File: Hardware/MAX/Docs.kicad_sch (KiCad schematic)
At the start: 0 parts

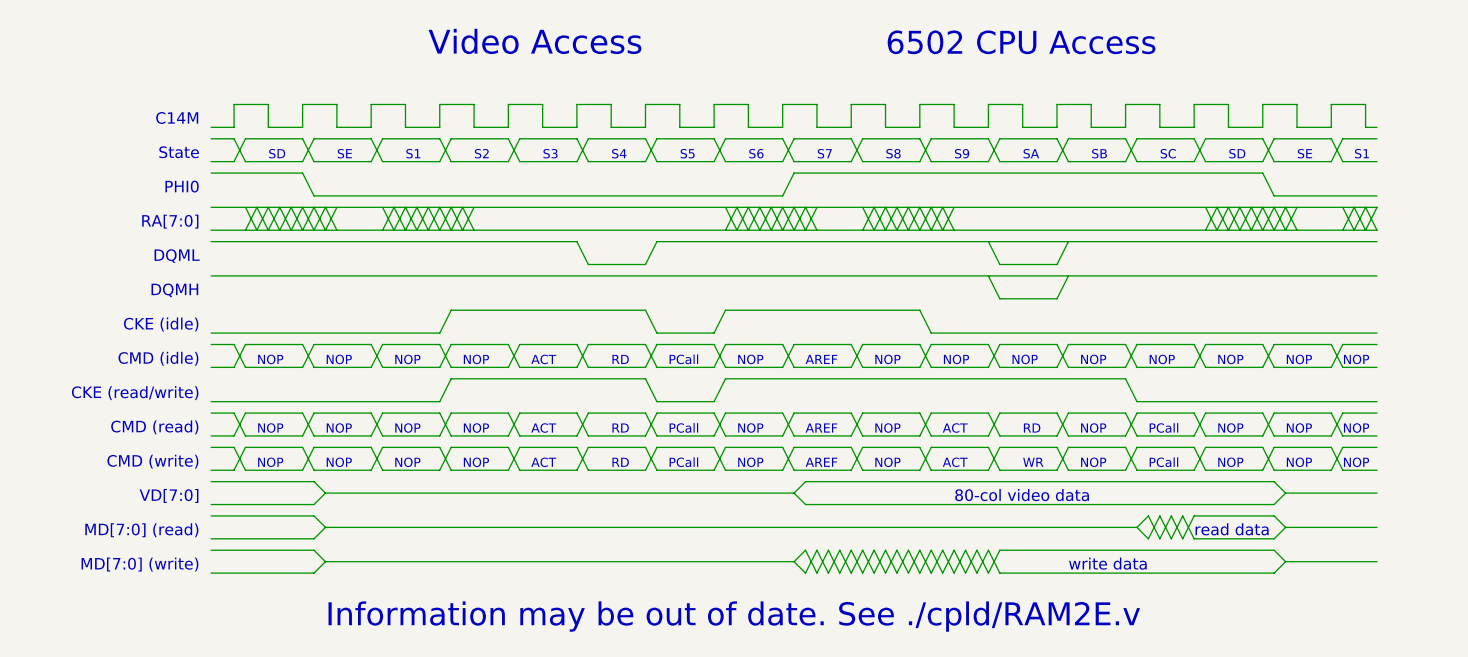
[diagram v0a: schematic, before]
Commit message: Revert "As sent to testers"
This reverts commit 4249ebe98332ad6fb679362fa153720a3e50f79b.
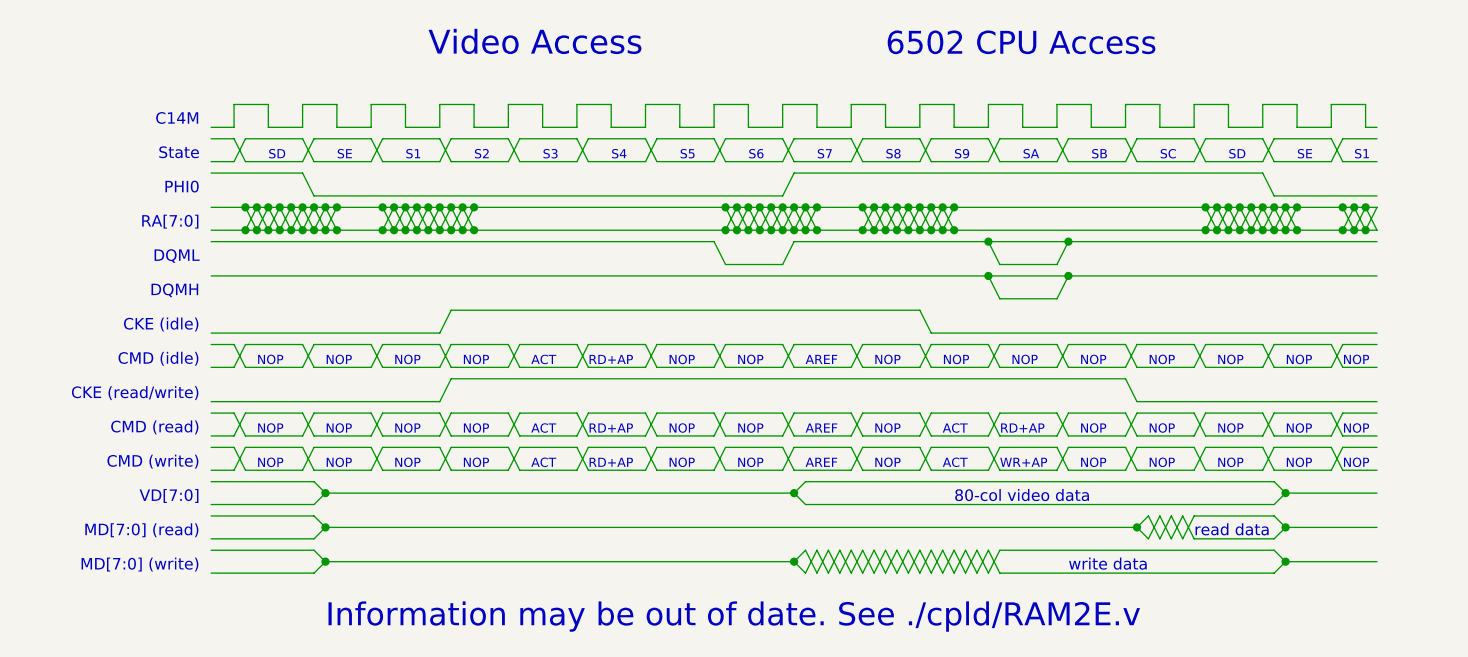
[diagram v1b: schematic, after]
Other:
- note added: "RD+AP"
- note added: "WR+AP"
- note removed: "PCall"
- note removed: "RD"
- note removed: "WR"
